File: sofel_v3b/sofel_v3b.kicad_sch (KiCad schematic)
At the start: 76 parts, among them J1 Pimaroni Trackball, J2 4PIN, J3 OLED, J4 Conn_01x05_Socket, SW1 SW_PUSH_LED, SW10 SW_PUSH_LED, SW11 SW_PUSH_LED, SW12 SW_PUSH_LED, SW13 SW_PUSH_LED, SW14 SW_PUSH_LED, SW15 SW_PUSH_LED, SW16 SW_PUSH_LED, SW17 SW_PUSH_LED, SW18 SW_PUSH_LED, SW19 SW_PUSH_LED, SW2 SW_PUSH_LED, SW20 SW_PUSH_LED, SW21 SW_PUSH_LED, SW22 SW_PUSH_LED, SW23 SW_PUSH_LED, SW24 SW_PUSH_LED, SW25 Rotary_Encoder_Switch, SW26 SW_PUSH_LED, SW27 SW_PUSH_LED, SW28 SW_PUSH_LED, SW29 SW_PUSH_LED, SW3 SW_PUSH_LED, SW30 SW_PUSH_LED, SW4 SW_PUSH_LED, SW5 SW_PUSH_LED, SW6 SW_PUSH_LED, SW7 SW_PUSH_LED, SW8 SW_PUSH_LED, SW9 SW_PUSH_LED, U2 SN74AHCT1G125, U3 Pico

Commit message: Updated OLED footprint to support multiple models
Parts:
- J3: footprint sofle_v3b:OLED SSD1306 128x64 UNVERIFIED -> sofle_v3b:OLED SSD1306 128x64 UNVERIFIED v2
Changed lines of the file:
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@@
       (effects (font (size 1.27 1.27)))
     )
-    (property "Footprint" "sofle_v3b:OLED SSD1306 128x64 UNVERIFIED" (at 71.12 163.83 0)
+    (property "Footprint" "sofle_v3b:OLED SSD1306 128x64 UNVERIFIED v2" (at 71.12 163.83 0)
       (effects (font (size 1.27 1.27)) hide)
     )

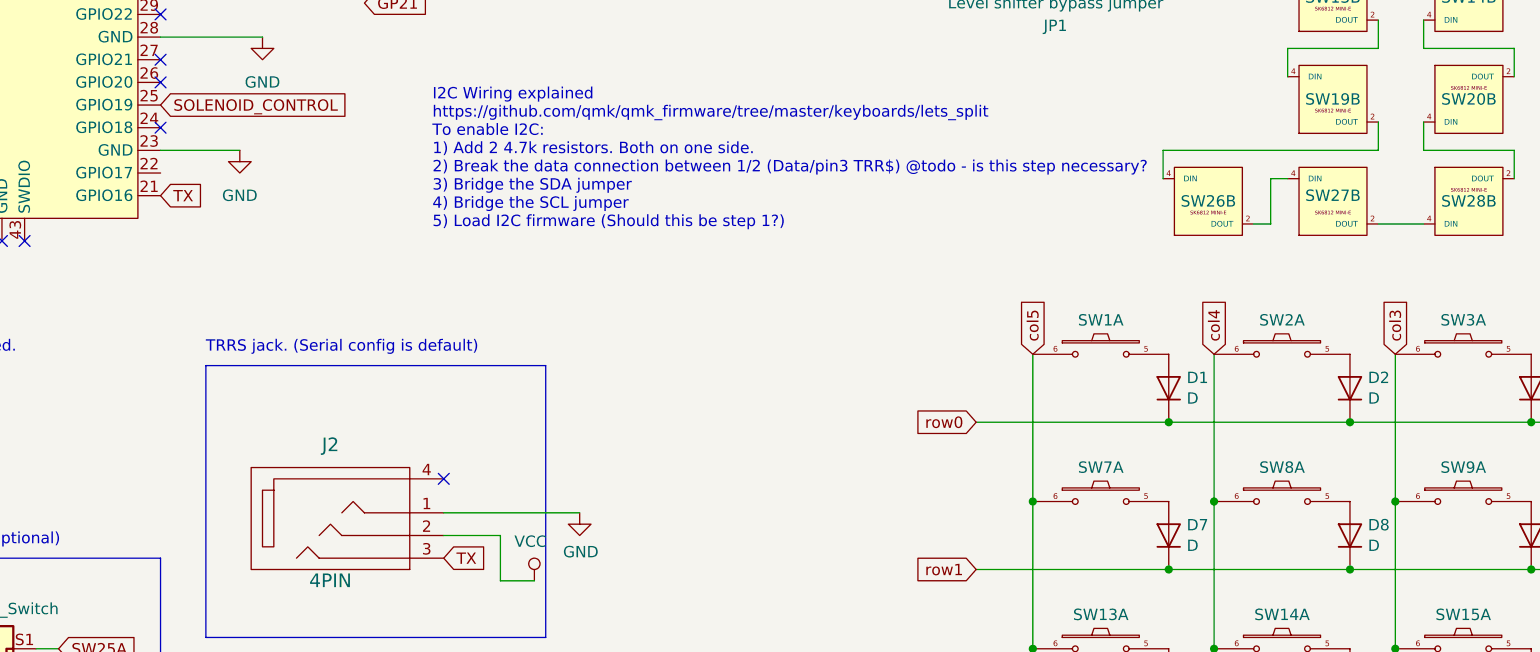
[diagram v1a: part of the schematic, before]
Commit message: Added full duplex wiring support w/ tx rx firmware crossover
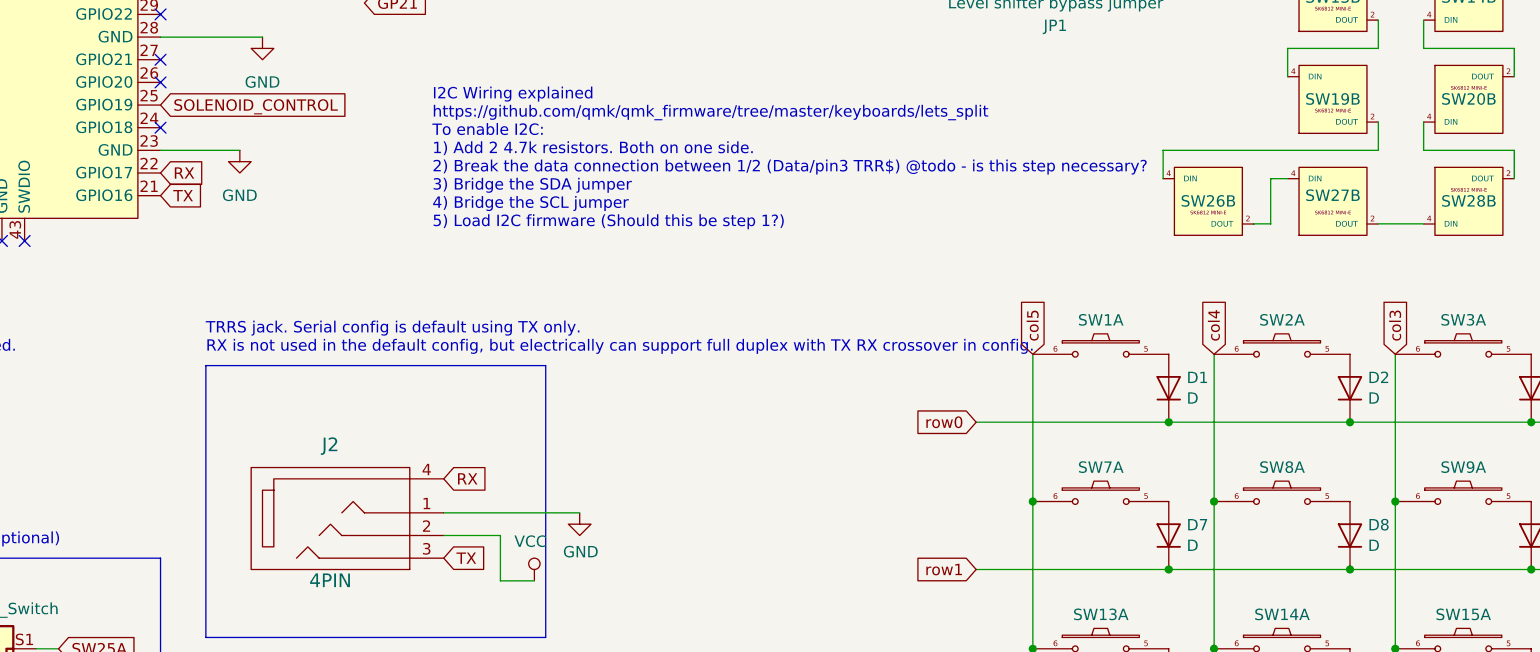
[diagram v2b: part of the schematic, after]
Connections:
- net RX: now reaches J2.4
- net RX: now also U3.22 (GPIO17)
- no-connect marks 17 -> 16
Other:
- note added: "TRRS jack. Serial config is default using TX only. RX is not used in the default config, but electrically can support full duplex with TX RX crossover in config."
- note removed: "TRRS jack. (Serial config is default)"
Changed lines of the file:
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@@
   (no_connect (at 62.23 62.23))
   (no_connect (at 44.45 74.93))
-  (no_connect (at 93.98 101.6))
   (no_connect (at 62.23 29.21))
   (no_connect (at 41.91 74.93))
@@
     (effects (font (size 1.27 1.27)) (justify left bottom))
   )
-  (text "TRRS jack. (Serial config is default)" (at 67.31 87.63 0)
+  (text "TRRS jack. Serial config is default using TX only. \nRX is not used in the default config, but electrically can support full duplex with TX RX crossover in config.\n"
+    (at 67.31 87.63 0)
     (effects (font (size 1.27 1.27)) (justify left bottom))
   )
@@
     )
   )
+  (global_label "RX" (shape input) (at 62.23 67.31 0) (fields_autoplaced)
+    (effects (font (size 1.27 1.27)) (justify left))
+    (property "Intersheetrefs" "${INTERSHEET_REFS}" (at 66.9611 67.31 0)
+      (effects (font (size 1.27 1.27)) (justify left) hide)
+    )
+  )
   (global_label "col1" (shape input) (at 26.67 29.21 180)
     (effects (font (size 1.27 1.27)) (justify right))
@@
     )
   )
+  (global_label "RX" (shape input) (at 93.98 101.6 0) (fields_autoplaced)
+    (effects (font (size 1.27 1.27)) (justify left))
+    (property "Intersheetrefs" "${INTERSHEET_REFS}" (at 98.7111 101.6 0)
+      (effects (font (size 1.27 1.27)) (justify left) hide)
+    )
+  )

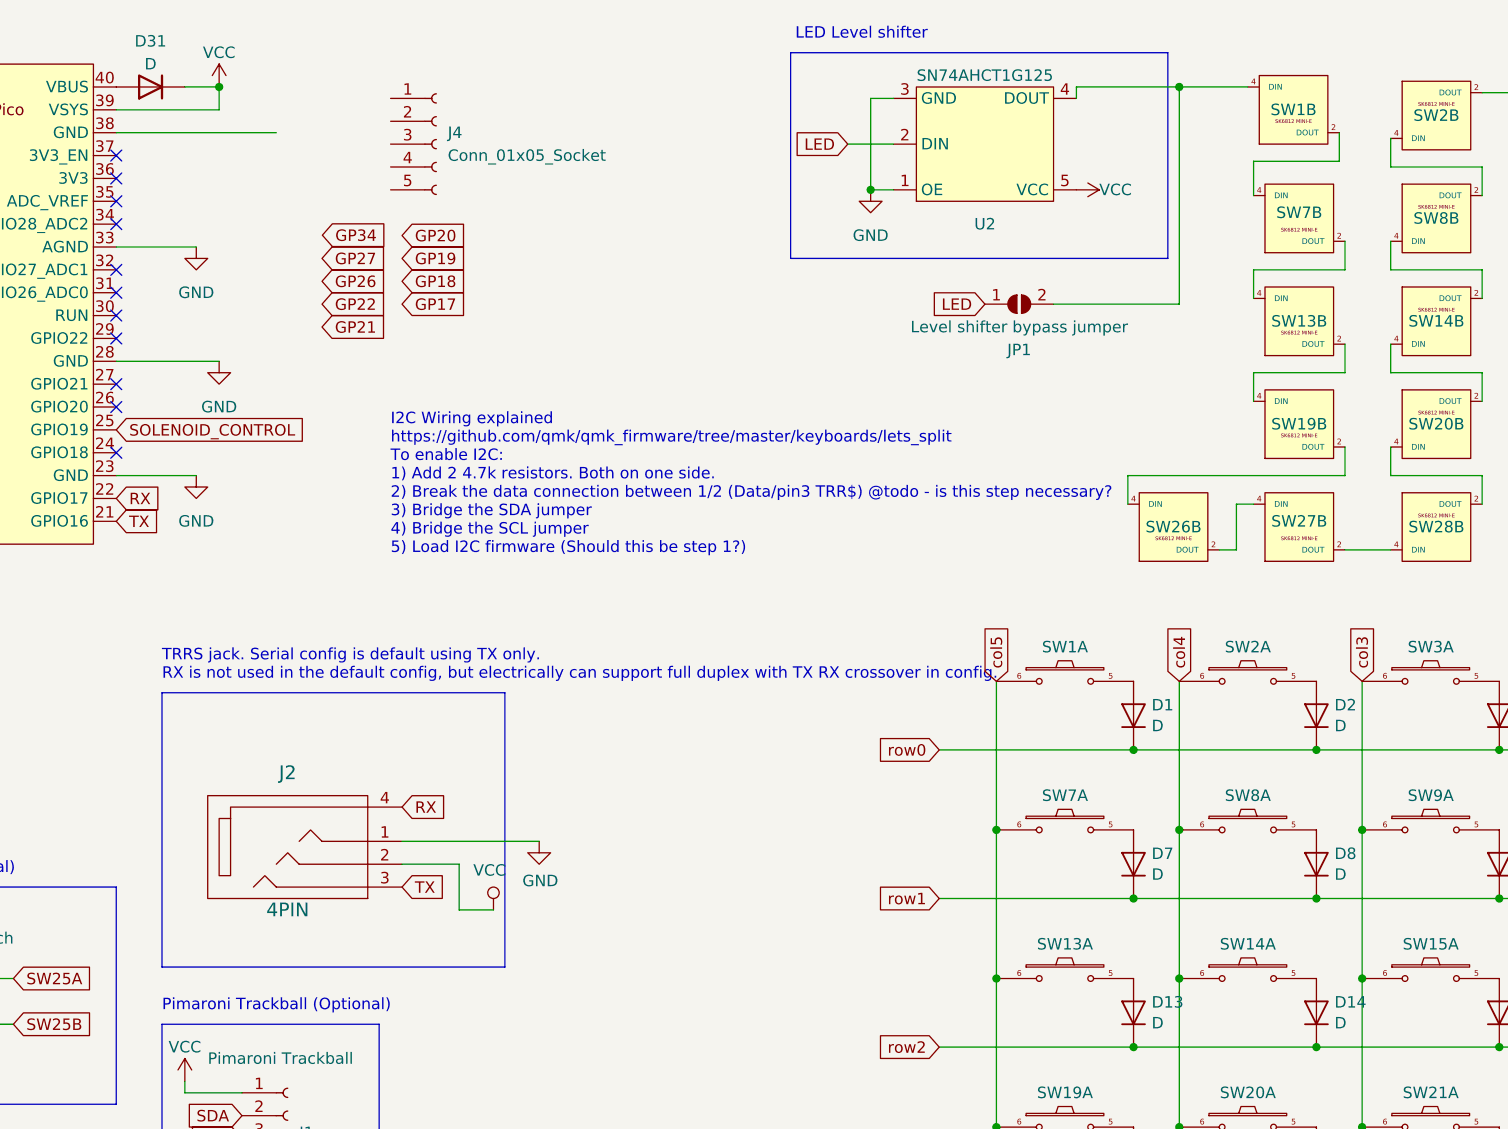
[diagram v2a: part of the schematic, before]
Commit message: updated keyplate for alternate OLEDs
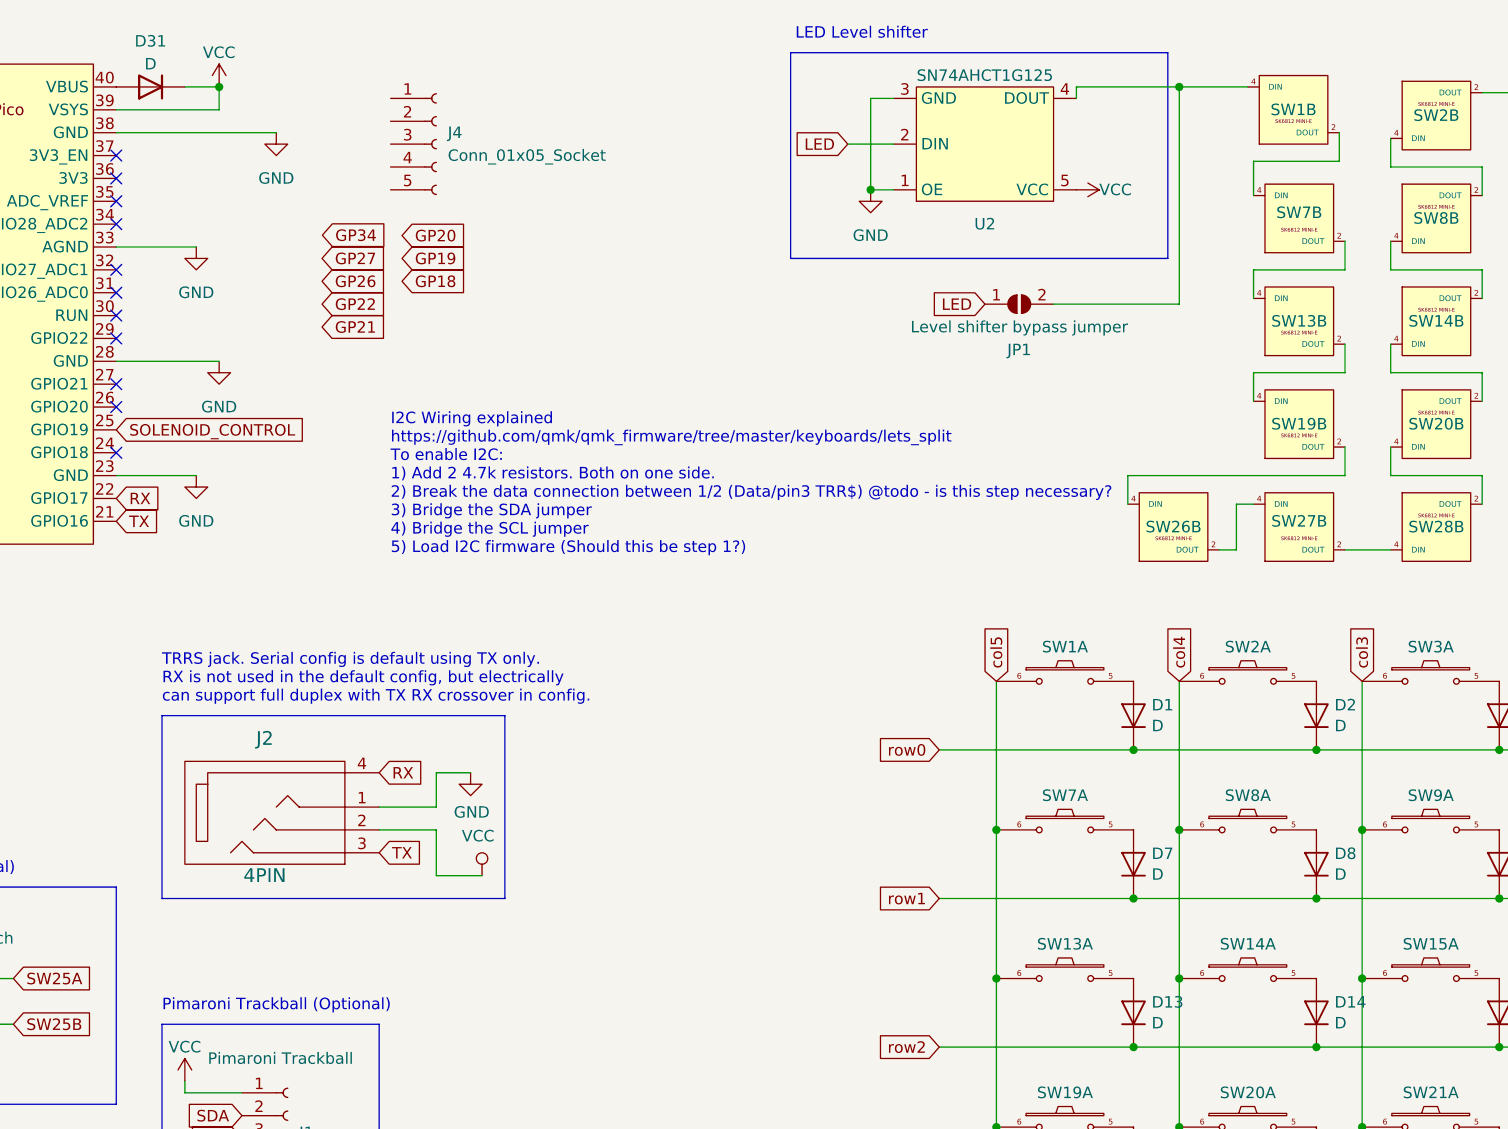
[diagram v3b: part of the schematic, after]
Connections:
- net GND: now also U3.38 (GND)
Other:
- moved on the sheet: J2
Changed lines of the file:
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@@
     (stroke (width 0) (type default))
   )
-  (wire (pts (xy 100.33 107.95) (xy 100.33 113.03))
+  (wire (pts (xy 97.79 104.14) (xy 97.79 109.22))
     (stroke (width 0) (type default))
   )
@@
     (stroke (width 0) (type default))
   )
+  (wire (pts (xy 97.79 97.79) (xy 97.79 101.6))
+    (stroke (width 0) (type default))
+  )
   (wire (pts (xy 198.755 41.91) (xy 188.595 41.91))
     (stroke (width 0) (type default))
@@
     (stroke (width 0) (type default))
   )
-  (wire (pts (xy 93.98 107.95) (xy 100.33 107.95))
+  (wire (pts (xy 91.44 104.14) (xy 97.79 104.14))
     (stroke (width 0) (type default))
   )
@@
     (stroke (width 0) (type default))
   )
+  (wire (pts (xy 97.79 101.6) (xy 91.44 101.6))
+    (stroke (width 0) (type default))
+  )
   (wire (pts (xy 195.58 95.25) (xy 215.9 95.25))
     (stroke (width 0) (type default))
@@
     (stroke (width 0) (type default))
   )
-  (wire (pts (xy 93.98 105.41) (xy 109.22 105.41))
+  (wire (pts (xy 97.79 97.79) (xy 101.6 97.79))
     (stroke (width 0) (type default))
   )
@@
     (stroke (width 0) (type default))
   )
-  (wire (pts (xy 100.33 113.03) (xy 104.14 113.03))
+  (wire (pts (xy 97.79 109.22) (xy 102.87 109.22))
     (stroke (width 0) (type default))
   )
@@
     (fill (type none))
   )
-  (rectangle (start 67.31 88.9) (end 105.41 119.38)
+  (rectangle (start 67.31 91.44) (end 105.41 111.76)
     (stroke (width 0) (type default))
     (fill (type none))
@@
     (effects (font (size 1.27 1.27)) (justify left bottom))
   )
-  (text "TRRS jack. Serial config is default using TX only. \nRX is not used in the default config, but electrically can support full duplex with TX RX crossover in config.\n"
-    (at 67.31 87.63 0)
+  (text "TRRS jack. Serial config is default using TX only. \nRX is not used in the default config, but electrically \ncan support full duplex with TX RX crossover in config.\n"
+    (at 67.31 90.17 0)
     (effects (font (size 1.27 1.27)) (justify left bottom))
   )
@@
     )
   )
-  (global_label "TX" (shape input) (at 93.98 110.49 0) (fields_autoplaced)
+  (global_label "TX" (shape input) (at 91.44 106.68 0) (fields_autoplaced)
     (effects (font (size 1.27 1.27)) (justify left))
-    (property "Intersheetrefs" "${INTERSHEET_REFS}" (at 98.4087 110.49 0)
+    (property "Intersheetrefs" "${INTERSHEET_REFS}" (at 95.8687 106.68 0)
       (effects (font (size 1.27 1.27)) (justify left) hide)
     )
@@
     )
   )
-  (global_label "GP17" (shape input) (at 93.98 45.72 0) (fields_autoplaced)
-    (effects (font (size 1.27 1.27)) (justify left))
-    (property "Intersheetrefs" "${INTERSHEET_REFS}" (at 101.1906 45.72 0)
-      (effects (font (size 1.27 1.27)) (justify left) hide)
-    )
-  )
   (global_label "LED" (shape input) (at 143.51 27.94 180) (fields_autoplaced)
     (effects (font (size 1.27 1.27)) (justify right))
@@
     )
   )
-  (global_label "RX" (shape input) (at 93.98 101.6 0) (fields_autoplaced)
+  (global_label "RX" (shape input) (at 91.44 97.79 0) (fields_autoplaced)
     (effects (font (size 1.27 1.27)) (justify left))
-    (property "Intersheetrefs" "${INTERSHEET_REFS}" (at 98.7111 101.6 0)
+    (property "Intersheetrefs" "${INTERSHEET_REFS}" (at 96.1711 97.79 0)
       (effects (font (size 1.27 1.27)) (justify left) hide)
     )
@@
     )
   )
-  (symbol (lib_id "SofleKeyboard-rescue:MJ-4PP-9-Lily58-cache-Lily58_Pro-rescue") (at 82.55 105.41 0) (unit 1)
+  (symbol (lib_id "SofleKeyboard-rescue:MJ-4PP-9-Lily58-cache-Lily58_Pro-rescue") (at 80.01 101.6 0) (unit 1)
     (in_bom yes) (on_board yes) (dnp no)
-    (property "Reference" "J2" (at 81.28 97.79 0)
+    (property "Reference" "J2" (at 78.74 93.98 0)
       (effects (font (size 1.524 1.524)))
     )
-    (property "Value" "4PIN" (at 81.28 113.03 0)
+    (property "Value" "4PIN" (at 78.74 109.22 0)
       (effects (font (size 1.524 1.524)))
     )
-    (property "Footprint" "sofle_v3b:MJ-4PP-9" (at 82.55 106.68 0)
+    (property "Footprint" "sofle_v3b:MJ-4PP-9" (at 80.01 102.87 0)
       (effects (font (size 1.524 1.524)) hide)
     )
-    (property "Datasheet" "" (at 82.55 106.68 0)
+    (property "Datasheet" "" (at 80.01 102.87 0)
       (effects (font (size 1.524 1.524)))
     )
@@
     )
   )
+  (symbol (lib_id "power:GND") (at 80.01 26.67 0) (unit 1)
+    (in_bom yes) (on_board yes) (dnp no) (fields_autoplaced)
+    (property "Reference" "#PWR09" (at 80.01 33.02 0)
+      (effects (font (size 1.27 1.27)) hide)
+    )
+    (property "Value" "GND" (at 80.01 31.75 0)
+      (effects (font (size 1.27 1.27)))
+    )
+    (property "Footprint" "" (at 80.01 26.67 0)
+      (effects (font (size 1.27 1.27)) hide)
+    )
+    (property "Datasheet" "" (at 80.01 26.67 0)
+      (effects (font (size 1.27 1.27)) hide)
+    )
+    (pin "1")
+    (instances
+      (project "sofel_v3b"
+        (path "/06057b3a-55ab-4f4e-913e-2aeec5ff3587"
+          (reference "#PWR09") (unit 1)
+        )
+      )
+      (project "Sofle_v3"
+        (path "/aae4773e-62e9-4e6e-acb6-89e78a092249"
+          (reference "#PWR018") (unit 1)
+        )
+      )
+    )
+  )
   (symbol (lib_id "power:VCC") (at 168.91 33.02 270) (unit 1)
     (in_bom yes) (on_board yes) (dnp no)
@@
     )
   )
-  (symbol (lib_id "SofleKeyboard-rescue:GND-power") (at 109.22 105.41 0) (unit 1)
+  (symbol (lib_id "SofleKeyboard-rescue:GND-power") (at 101.6 97.79 0) (unit 1)
     (in_bom yes) (on_board yes) (dnp no)
-    (property "Reference" "#PWR02" (at 109.22 111.76 0)
+    (property "Reference" "#PWR02" (at 101.6 104.14 0)
       (effects (font (size 1.27 1.27)) hide)
     )
-    (property "Value" "GND" (at 109.347 109.8042 0)
+    (property "Value" "GND" (at 101.727 102.1842 0)
       (effects (font (size 1.27 1.27)))
     )
-    (property "Footprint" "" (at 109.22 105.41 0)
+    (property "Footprint" "" (at 101.6 97.79 0)
       (effects (font (size 1.27 1.27)) hide)
     )
-    (property "Datasheet" "" (at 109.22 105.41 0)
+    (property "Datasheet" "" (at 101.6 97.79 0)
       (effects (font (size 1.27 1.27)) hide)
     )
@@
     )
   )
-  (symbol (lib_id "SofleKeyboard-rescue:VCC-power") (at 104.14 113.03 0) (mirror y) (unit 1)
+  (symbol (lib_id "SofleKeyboard-rescue:VCC-power") (at 102.87 109.22 0) (mirror y) (unit 1)
     (in_bom yes) (on_board yes) (dnp no)
-    (property "Reference" "#PWR01" (at 104.14 116.84 0)
+    (property "Reference" "#PWR01" (at 102.87 113.03 0)
       (effects (font (size 1.27 1.27)) hide)
     )
-    (property "Value" "VCC" (at 103.7082 108.6358 0)
+    (property "Value" "VCC" (at 102.4382 104.8258 0)
       (effects (font (size 1.27 1.27)))
     )
-    (property "Footprint" "" (at 104.14 113.03 0)
+    (property "Footprint" "" (at 102.87 109.22 0)
       (effects (font (size 1.27 1.27)) hide)
     )
-    (property "Datasheet" "" (at 104.14 113.03 0)
+    (property "Datasheet" "" (at 102.87 109.22 0)
       (effects (font (size 1.27 1.27)) hide)
     )

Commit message: Flipped pico footrpint so buttons face up Removed pcb holes for pico buttons
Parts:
- U3: footprint sofle_v3b:RPi_Pico_SMD_TH - Junco -DS Sofle v3b v4 -> sofle_v3b:RPi_Pico_SMD_TH - Junco -DS Sofle v3b v3 nohole
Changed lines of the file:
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@@
       (effects (font (size 1.27 1.27)))
     )
-    (property "Footprint" "sofle_v3b:RPi_Pico_SMD_TH - Junco -DS Sofle v3b v4" (at 44.45 45.72 90)
+    (property "Footprint" "sofle_v3b:RPi_Pico_SMD_TH - Junco -DS Sofle v3b v3 nohole" (at 44.45 45.72 90)
       (effects (font (size 1.27 1.27)) hide)
     )
